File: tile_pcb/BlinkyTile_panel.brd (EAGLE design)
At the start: 220.1 x 170 mm, 210 parts

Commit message: Rev M panel from Sam
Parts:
- removed C1: .1uF, adafruit:C0603
- removed E$1, E$10, E$11, E$12, E$13, E$14, E$15, E$2, E$21, E$22, E$3, E$4, E$47, E$48, E$5, E$55, E$6, E$7, E$8, E$9: (no value), dodocohedreled:MOUSE_BITE_1
- removed E$16, E$17, E$19, E$20: (no value), dodocohedreled:MOUSE_BITE
- removed E$18: (no value), Sam-Lib:DUPONT-4P
- removed PROG, PROG1: (no value), solpad:SE14
- removed R1: 75, adafruit:R0603
- removed R2: 10k, adafruit:R0603
- removed U$2, U$3, U$4, U$5, U$6, U$91: D_EDGEMOD, dodocohedreled:D_EDGE_SLOT_MOD
- removed U$7: WS2822S_LED, blinkinlabs:WS2822S_LED
- added C4: .1uF, adafruit:C0603
- added E$100, E$101, E$102, E$103, E$104, E$105, E$106, E$107, E$108, E$109, E$110, E$111, E$112, E$113, E$114, E$115, E$116, E$117, E$118, E$119, E$120, E$121, E$122, E$123, E$124, E$125, E$126, E$127, E$128, E$129, E$130, E$131, E$132, E$133, E$134, E$135, E$136, E$137, E$138, E$139, E$140, E$141, E$142, E$143, E$144, E$145, E$146, E$147, E$148, E$149, E$150, E$151, E$152, E$153, E$154, E$155, E$156, E$157, E$158, E$159, E$160, E$161, E$162, E$163, E$164, E$165, E$166, E$167, E$168, E$169, E$170, E$171, E$172, E$173, E$174, E$175, E$176, E$177, E$178, E$179, E$180, E$181, E$182, E$183, E$184, E$185, E$186, E$187, E$188, E$189, E$190, E$191, E$192, E$193, E$199, E$200, E$202, E$203, E$81, E$82, E$83, E$84, E$85, E$86, E$87, E$88, E$89, E$90, E$91, E$92, E$93, E$94, E$95, E$96, E$97, E$98, E$99: (no value), dodocohedreled:MOUSE_BITE_1
- added E$201, E$204: (no value), dodocohedreled:4-PIN_DUPONT
- added E$205, E$206, E$207, E$208, E$209, E$210, E$211, E$212, E$213, E$214, E$215, E$216, E$217, E$218: (no value), dodocohedreled:BLINKYTILE
- added E$219: (no value), dodocohedreled:BLINKYTILELOGO
- added E$220, E$225: (no value), dodocohedreled:BLINKINLABSLOGO
- added E$221, E$222, E$223, E$224: (no value), SparkFun-Aesthetics:FIDUCIAL-1X2
- added PROG2, PROG3: (no value), solpad:SE14
- added R7: 75, adafruit:R0603
- added R8: 10k, adafruit:R0603
- added U$20, U$21, U$22, U$23, U$93, U$94: D_EDGEMOD, dodocohedreled:D_EDGE_SLOT_MOD
- added U$24: WS2822S_LED, blinkinlabs:WS2822S_LED
- E$76: device Sam-Lib:DUPONT-4P -> dodocohedreled:MOUSE_BITE_1
- E$77, E$78, E$79, E$80: device SparkFun-Aesthetics:FIDUCIAL-1X2 -> dodocohedreled:MOUSE_BITE_1
- moved E$67 207.0 mm to (105.3, 30.9), turned to 288 degrees
- moved E$80 202.4 mm to (78.3, 52.4), turned to 252 degrees
- moved E$70 188.5 mm to (81.0, 48.5), turned to 0 degrees
- moved E$73 184.2 mm to (81.0, 48.5), turned to 0 degrees
- moved U$44 182.5 mm to (-74.2, 66.8), turned to 252 degrees
- moved U$86 182.5 mm to (74.2, -66.8), turned to 72 degrees
- moved E$32 181.3 mm to (-105.3, 30.9), turned to 72 degrees
- moved E$72 174.3 mm to (105.3, 30.9), turned to 288 degrees
- moved E$78 164.8 mm to (39.0, 80.9), turned to 36 degrees
- moved U$46 160.0 mm to (-66.5, 43.0), turned to 324 degrees
- moved U$88 160.0 mm to (66.5, -43.0), turned to 144 degrees
- moved E$71 159.1 mm to (56.7, 30.9), turned to 72 degrees
- moved E$74 158.8 mm to (29.7, 52.4)
- moved U$43 156.7 mm to (-54.0, 81.5), turned to 180 degrees
- moved U$85 156.7 mm to (54.0, -81.5), turned to 0 degrees
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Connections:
- removed net 5V: R1.1, U$2.P$2, U$2.P$4, U$2.P$7, U$2.P$9, U$2.PWRVIA1, U$2.PWRVIA3, U$2.PWRVIA4, U$2.PWRVIA6, U$3.P$2, U$3.P$4, U$3.P$7, U$3.P$9, U$3.PWRVIA1, U$3.PWRVIA3, U$3.PWRVIA4, U$3.PWRVIA6, U$4.P$2, U$4.P$4, U$4.P$7, U$4.P$9, U$4.PWRVIA1, U$4.PWRVIA3, U$4.PWRVIA4, U$4.PWRVIA6, U$5.P$2, U$5.P$4, U$5.P$7, U$5.P$9, U$5.PWRVIA1, U$5.PWRVIA3, U$5.PWRVIA4, U$5.PWRVIA6, U$6.P$2, U$6.P$4, U$6.P$7, U$6.P$9, U$6.PWRVIA1, U$6.PWRVIA3, U$6.PWRVIA4, U$6.PWRVIA6, U$7.6
- removed net 5V1: R3.1, U$1.P$2, U$1.P$4, U$1.P$7, U$1.P$9, U$1.PWRVIA1, U$1.PWRVIA3, U$1.PWRVIA4, U$1.PWRVIA6, U$10.P$2, U$10.P$4, U$10.P$7, U$10.P$9, U$10.PWRVIA1, U$10.PWRVIA3, U$10.PWRVIA4, U$10.PWRVIA6, U$11.P$2, U$11.P$4, U$11.P$7, U$11.P$9, U$11.PWRVIA1, U$11.PWRVIA3, U$11.PWRVIA4, U$11.PWRVIA6, U$12.6, U$8.P$2, U$8.P$4, U$8.P$7, U$8.P$9, U$8.PWRVIA1, U$8.PWRVIA3, U$8.PWRVIA4, U$8.PWRVIA6, U$9.P$2, U$9.P$4, U$9.P$7, U$9.P$9, U$9.PWRVIA1, U$9.PWRVIA3, U$9.PWRVIA4, U$9.PWRVIA6
- removed net ADRI: U$7.2
- removed net DATA: R2.2, U$2.P$3, U$2.P$8, U$2.SIGVIA1, U$2.SIGVIA3, U$3.P$3, U$3.P$8, U$3.SIGVIA1, U$3.SIGVIA3, U$4.P$3, U$4.P$8, U$4.SIGVIA1, U$4.SIGVIA3, U$5.P$3, U$5.P$8, U$5.SIGVIA1, U$5.SIGVIA3, U$6.P$3, U$6.P$8, U$6.SIGVIA1, U$6.SIGVIA3
- removed net GND: C1.2, U$2.GNDVIA1, U$2.GNDVIA3, U$2.GNDVIA4, U$2.GNDVIA6, U$2.P$1, U$2.P$10, U$2.P$5, U$2.P$6, U$3.GNDVIA1, U$3.GNDVIA3, U$3.GNDVIA4, U$3.GNDVIA6, U$3.P$1, U$3.P$10, U$3.P$5, U$3.P$6, U$4.GNDVIA1, U$4.GNDVIA3, U$4.GNDVIA4, U$4.GNDVIA6, U$4.P$1, U$4.P$10, U$4.P$5, U$4.P$6, U$5.GNDVIA1, U$5.GNDVIA3, U$5.GNDVIA4, U$5.GNDVIA6, U$5.P$1, U$5.P$10, U$5.P$5, U$5.P$6, U$6.GNDVIA1, U$6.GNDVIA3, U$6.GNDVIA4, U$6.GNDVIA6, U$6.P$1, U$6.P$10, U$6.P$5, U$6.P$6, U$7.4
- removed net N$1: C1.1, R1.2, U$7.3
- removed net N$2: R2.1, U$7.1
- removed net S$1: E$18.P$2, U$91.P$3
- removed net S$10: E$18.P$3, PROG.MP
- removed net S$2: E$18.P$4, U$91.P$1, U$91.P$5
- removed net S$3: E$76.P$4, U$19.P$1, U$19.P$5
- removed net S$4: E$76.P$2, U$19.P$3
- removed net S$5: E$76.P$3, PROG1.MP
- removed net VCC: E$18.P$1, U$91.P$7, U$91.P$9
- removed net VCC1: E$76.P$1, U$19.P$7, U$19.P$9
- new net 5V15: R29.1, U$85.P$2, U$85.P$4, U$85.P$7, U$85.P$9, U$85.PWRVIA1, U$85.PWRVIA3, U$85.PWRVIA4, U$85.PWRVIA6, U$86.P$2, U$86.P$4, U$86.P$7, U$86.P$9, U$86.PWRVIA1, U$86.PWRVIA3, U$86.PWRVIA4, U$86.PWRVIA6, U$87.P$2, U$87.P$4, U$87.P$7, U$87.P$9, U$87.PWRVIA1, U$87.PWRVIA3, U$87.PWRVIA4, U$87.PWRVIA6, U$88.P$2, U$88.P$4, U$88.P$7, U$88.P$9, U$88.PWRVIA1, U$88.PWRVIA3, U$88.PWRVIA4, U$88.PWRVIA6, U$89.P$2, U$89.P$4, U$89.P$7, U$89.P$9, U$89.PWRVIA1, U$89.PWRVIA3, U$89.PWRVIA4, U$89.PWRVIA6, U$90.6
- new net 5V3: R5.1, U$13.P$2, U$13.P$4, U$13.P$7, U$13.P$9, U$13.PWRVIA1, U$13.PWRVIA3, U$13.PWRVIA4, U$13.PWRVIA6, U$14.P$2, U$14.P$4, U$14.P$7, U$14.P$9, U$14.PWRVIA1, U$14.PWRVIA3, U$14.PWRVIA4, U$14.PWRVIA6, U$15.P$2, U$15.P$4, U$15.P$7, U$15.P$9, U$15.PWRVIA1, U$15.PWRVIA3, U$15.PWRVIA4, U$15.PWRVIA6, U$16.P$2, U$16.P$4, U$16.P$7, U$16.P$9, U$16.PWRVIA1, U$16.PWRVIA3, U$16.PWRVIA4, U$16.PWRVIA6, U$17.P$2, U$17.P$4, U$17.P$7, U$17.P$9, U$17.PWRVIA1, U$17.PWRVIA3, U$17.PWRVIA4, U$17.PWRVIA6, U$18.6
- new net ADRI3: U$24.2
- new net DATA3: R8.2, U$19.P$3, U$19.P$8, U$19.SIGVIA1, U$19.SIGVIA3, U$20.P$3, U$20.P$8, U$20.SIGVIA1, U$20.SIGVIA3, U$21.P$3, U$21.P$8, U$21.SIGVIA1, U$21.SIGVIA3, U$22.P$3, U$22.P$8, U$22.SIGVIA1, U$22.SIGVIA3, U$23.P$3, U$23.P$8, U$23.SIGVIA1, U$23.SIGVIA3
- new net GND3: C4.2, U$19.GNDVIA1, U$19.GNDVIA3, U$19.GNDVIA4, U$19.GNDVIA6, U$19.P$1, U$19.P$10, U$19.P$5, U$19.P$6, U$20.GNDVIA1, U$20.GNDVIA3, U$20.GNDVIA4, U$20.GNDVIA6, U$20.P$1, U$20.P$10, U$20.P$5, U$20.P$6, U$21.GNDVIA1, U$21.GNDVIA3, U$21.GNDVIA4, U$21.GNDVIA6, U$21.P$1, U$21.P$10, U$21.P$5, U$21.P$6, U$22.GNDVIA1, U$22.GNDVIA3, U$22.GNDVIA4, U$22.GNDVIA6, U$22.P$1, U$22.P$10, U$22.P$5, U$22.P$6, U$23.GNDVIA1, U$23.GNDVIA3, U$23.GNDVIA4, U$23.GNDVIA6, U$23.P$1, U$23.P$10, U$23.P$5, U$23.P$6, U$24.4
- new net N$11: C4.1, R7.2, U$24.3
- new net N$12: R8.1, U$24.1
- new net S$11: E$204.P$2, U$94.P$3
- new net S$12: E$204.P$3, PROG3.MP
- new net S$6: E$201.P$4, U$93.P$1, U$93.P$5
- new net S$7: E$201.P$2, U$93.P$3
- new net S$8: E$201.P$3, PROG2.MP
- new net S$9: E$204.P$4, U$94.P$1, U$94.P$5
- new net VCC2: E$201.P$1, U$93.P$7, U$93.P$9
- new net VCC3: E$204.P$1, U$94.P$7, U$94.P$9
- net 5V10: now also R19.1, U$55.P$2, U$55.P$4, U$55.P$7, U$55.P$9, U$55.PWRVIA1, U$55.PWRVIA3, U$55.PWRVIA4, U$55.PWRVIA6, U$56.P$2, U$56.P$4, U$56.P$7, U$56.P$9, U$56.PWRVIA1, U$56.PWRVIA3, U$56.PWRVIA4, U$56.PWRVIA6, U$57.P$2, U$57.P$4, U$57.P$7, U$57.P$9, U$57.PWRVIA1, U$57.PWRVIA3, U$57.PWRVIA4, U$57.PWRVIA6, U$58.P$2, U$58.P$4, U$58.P$7, U$58.P$9, U$58.PWRVIA1, U$58.PWRVIA3, U$58.PWRVIA4, U$58.PWRVIA6, U$59.P$2, U$59.P$4, U$59.P$7, U$59.P$9, U$59.PWRVIA1, U$59.PWRVIA3, U$59.PWRVIA4, U$59.PWRVIA6, U$60.6; no longer R21.1, U$61.P$2, U$61.P$4, U$61.P$7, U$61.P$9, U$61.PWRVIA1, U$61.PWRVIA3, U$61.PWRVIA4, U$61.PWRVIA6, U$62.P$2, U$62.P$4, U$62.P$7, U$62.P$9, U$62.PWRVIA1, U$62.PWRVIA3, U$62.PWRVIA4, U$62.PWRVIA6, U$63.P$2, U$63.P$4, U$63.P$7, U$63.P$9, U$63.PWRVIA1, U$63.PWRVIA3, U$63.PWRVIA4, U$63.PWRVIA6, U$64.P$2, U$64.P$4, U$64.P$7, U$64.P$9, U$64.PWRVIA1, U$64.PWRVIA3, U$64.PWRVIA4, U$64.PWRVIA6, U$65.P$2, U$65.P$4, U$65.P$7, U$65.P$9, U$65.PWRVIA1, U$65.PWRVIA3, U$65.PWRVIA4, U$65.PWRVIA6, U$66.6
- net 5V11: now also R21.1, U$61.P$2, U$61.P$4, U$61.P$7, U$61.P$9, U$61.PWRVIA1, U$61.PWRVIA3, U$61.PWRVIA4, U$61.PWRVIA6, U$62.P$2, U$62.P$4, U$62.P$7, U$62.P$9, U$62.PWRVIA1, U$62.PWRVIA3, U$62.PWRVIA4, U$62.PWRVIA6, U$63.P$2, U$63.P$4, U$63.P$7, U$63.P$9, U$63.PWRVIA1, U$63.PWRVIA3, U$63.PWRVIA4, U$63.PWRVIA6, U$64.P$2, U$64.P$4, U$64.P$7, U$64.P$9, U$64.PWRVIA1, U$64.PWRVIA3, U$64.PWRVIA4, U$64.PWRVIA6, U$65.P$2, U$65.P$4, U$65.P$7, U$65.P$9, U$65.PWRVIA1, U$65.PWRVIA3, U$65.PWRVIA4, U$65.PWRVIA6, U$66.6; no longer R23.1, U$67.P$2, U$67.P$4, U$67.P$7, U$67.P$9, U$67.PWRVIA1, U$67.PWRVIA3, U$67.PWRVIA4, U$67.PWRVIA6, U$68.P$2, U$68.P$4, U$68.P$7, U$68.P$9, U$68.PWRVIA1, U$68.PWRVIA3, U$68.PWRVIA4, U$68.PWRVIA6, U$69.P$2, U$69.P$4, U$69.P$7, U$69.P$9, U$69.PWRVIA1, U$69.PWRVIA3, U$69.PWRVIA4, U$69.PWRVIA6, U$70.P$2, U$70.P$4, U$70.P$7, U$70.P$9, U$70.PWRVIA1, U$70.PWRVIA3, U$70.PWRVIA4, U$70.PWRVIA6, U$71.P$2, U$71.P$4, U$71.P$7, U$71.P$9, U$71.PWRVIA1, U$71.PWRVIA3, U$71.PWRVIA4, U$71.PWRVIA6, U$72.6
- net 5V12: now also R23.1, U$67.P$2, U$67.P$4, U$67.P$7, U$67.P$9, U$67.PWRVIA1, U$67.PWRVIA3, U$67.PWRVIA4, U$67.PWRVIA6, U$68.P$2, U$68.P$4, U$68.P$7, U$68.P$9, U$68.PWRVIA1, U$68.PWRVIA3, U$68.PWRVIA4, U$68.PWRVIA6, U$69.P$2, U$69.P$4, U$69.P$7, U$69.P$9, U$69.PWRVIA1, U$69.PWRVIA3, U$69.PWRVIA4, U$69.PWRVIA6, U$70.P$2, U$70.P$4, U$70.P$7, U$70.P$9, U$70.PWRVIA1, U$70.PWRVIA3, U$70.PWRVIA4, U$70.PWRVIA6, U$71.P$2, U$71.P$4, U$71.P$7, U$71.P$9, U$71.PWRVIA1, U$71.PWRVIA3, U$71.PWRVIA4, U$71.PWRVIA6, U$72.6; no longer R25.1, U$73.P$2, U$73.P$4, U$73.P$7, U$73.P$9, U$73.PWRVIA1, U$73.PWRVIA3, U$73.PWRVIA4, U$73.PWRVIA6, U$74.P$2, U$74.P$4, U$74.P$7, U$74.P$9, U$74.PWRVIA1, U$74.PWRVIA3, U$74.PWRVIA4, U$74.PWRVIA6, U$75.P$2, U$75.P$4, U$75.P$7, U$75.P$9, U$75.PWRVIA1, U$75.PWRVIA3, U$75.PWRVIA4, U$75.PWRVIA6, U$76.P$2, U$76.P$4, U$76.P$7, U$76.P$9, U$76.PWRVIA1, U$76.PWRVIA3, U$76.PWRVIA4, U$76.PWRVIA6, U$77.P$2, U$77.P$4, U$77.P$7, U$77.P$9, U$77.PWRVIA1, U$77.PWRVIA3, U$77.PWRVIA4, U$77.PWRVIA6, U$78.6
- net 5V13: now also R25.1, U$73.P$2, U$73.P$4, U$73.P$7, U$73.P$9, U$73.PWRVIA1, U$73.PWRVIA3, U$73.PWRVIA4, U$73.PWRVIA6, U$74.P$2, U$74.P$4, U$74.P$7, U$74.P$9, U$74.PWRVIA1, U$74.PWRVIA3, U$74.PWRVIA4, U$74.PWRVIA6, U$75.P$2, U$75.P$4, U$75.P$7, U$75.P$9, U$75.PWRVIA1, U$75.PWRVIA3, U$75.PWRVIA4, U$75.PWRVIA6, U$76.P$2, U$76.P$4, U$76.P$7, U$76.P$9, U$76.PWRVIA1, U$76.PWRVIA3, U$76.PWRVIA4, U$76.PWRVIA6, U$77.P$2, U$77.P$4, U$77.P$7, U$77.P$9, U$77.PWRVIA1, U$77.PWRVIA3, U$77.PWRVIA4, U$77.PWRVIA6, U$78.6; no longer R27.1, U$79.P$2, U$79.P$4, U$79.P$7, U$79.P$9, U$79.PWRVIA1, U$79.PWRVIA3, U$79.PWRVIA4, U$79.PWRVIA6, U$80.P$2, U$80.P$4, U$80.P$7, U$80.P$9, U$80.PWRVIA1, U$80.PWRVIA3, U$80.PWRVIA4, U$80.PWRVIA6, U$81.P$2, U$81.P$4, U$81.P$7, U$81.P$9, U$81.PWRVIA1, U$81.PWRVIA3, U$81.PWRVIA4, U$81.PWRVIA6, U$82.P$2, U$82.P$4, U$82.P$7, U$82.P$9, U$82.PWRVIA1, U$82.PWRVIA3, U$82.PWRVIA4, U$82.PWRVIA6, U$83.P$2, U$83.P$4, U$83.P$7, U$83.P$9, U$83.PWRVIA1, U$83.PWRVIA3, U$83.PWRVIA4, U$83.PWRVIA6, U$84.6
- net 5V14: now also R27.1, U$79.P$2, U$79.P$4, U$79.P$7, U$79.P$9, U$79.PWRVIA1, U$79.PWRVIA3, U$79.PWRVIA4, U$79.PWRVIA6, U$80.P$2, U$80.P$4, U$80.P$7, U$80.P$9, U$80.PWRVIA1, U$80.PWRVIA3, U$80.PWRVIA4, U$80.PWRVIA6, U$81.P$2, U$81.P$4, U$81.P$7, U$81.P$9, U$81.PWRVIA1, U$81.PWRVIA3, U$81.PWRVIA4, U$81.PWRVIA6, U$82.P$2, U$82.P$4, U$82.P$7, U$82.P$9, U$82.PWRVIA1, U$82.PWRVIA3, U$82.PWRVIA4, U$82.PWRVIA6, U$83.P$2, U$83.P$4, U$83.P$7, U$83.P$9, U$83.PWRVIA1, U$83.PWRVIA3, U$83.PWRVIA4, U$83.PWRVIA6, U$84.6; no longer R29.1, U$85.P$2, U$85.P$4, U$85.P$7, U$85.P$9, U$85.PWRVIA1, U$85.PWRVIA3, U$85.PWRVIA4, U$85.PWRVIA6, U$86.P$2, U$86.P$4, U$86.P$7, U$86.P$9, U$86.PWRVIA1, U$86.PWRVIA3, U$86.PWRVIA4, U$86.PWRVIA6, U$87.P$2, U$87.P$4, U$87.P$7, U$87.P$9, U$87.PWRVIA1, U$87.PWRVIA3, U$87.PWRVIA4, U$87.PWRVIA6, U$88.P$2, U$88.P$4, U$88.P$7, U$88.P$9, U$88.PWRVIA1, U$88.PWRVIA3, U$88.PWRVIA4, U$88.PWRVIA6, U$89.P$2, U$89.P$4, U$89.P$7, U$89.P$9, U$89.PWRVIA1, U$89.PWRVIA3, U$89.PWRVIA4, U$89.PWRVIA6, U$90.6
- net 5V2: now also R3.1, U$1.P$2, U$1.P$4, U$1.P$7, U$1.P$9, U$1.PWRVIA1, U$1.PWRVIA3, U$1.PWRVIA4, U$1.PWRVIA6, U$10.P$2, U$10.P$4, U$10.P$7, U$10.P$9, U$10.PWRVIA1, U$10.PWRVIA3, U$10.PWRVIA4, U$10.PWRVIA6, U$11.P$2, U$11.P$4, U$11.P$7, U$11.P$9, U$11.PWRVIA1, U$11.PWRVIA3, U$11.PWRVIA4, U$11.PWRVIA6, U$12.6, U$8.P$2, U$8.P$4, U$8.P$7, U$8.P$9, U$8.PWRVIA1, U$8.PWRVIA3, U$8.PWRVIA4, U$8.PWRVIA6, U$9.P$2, U$9.P$4, U$9.P$7, U$9.P$9, U$9.PWRVIA1, U$9.PWRVIA3, U$9.PWRVIA4, U$9.PWRVIA6; no longer R5.1, U$13.P$2, U$13.P$4, U$13.P$7, U$13.P$9, U$13.PWRVIA1, U$13.PWRVIA3, U$13.PWRVIA4, U$13.PWRVIA6, U$14.P$2, U$14.P$4, U$14.P$7, U$14.P$9, U$14.PWRVIA1, U$14.PWRVIA3, U$14.PWRVIA4, U$14.PWRVIA6, U$15.P$2, U$15.P$4, U$15.P$7, U$15.P$9, U$15.PWRVIA1, U$15.PWRVIA3, U$15.PWRVIA4, U$15.PWRVIA6, U$16.P$2, U$16.P$4, U$16.P$7, U$16.P$9, U$16.PWRVIA1, U$16.PWRVIA3, U$16.PWRVIA4, U$16.PWRVIA6, U$17.P$2, U$17.P$4, U$17.P$7, U$17.P$9, U$17.PWRVIA1, U$17.PWRVIA3, U$17.PWRVIA4, U$17.PWRVIA6, U$18.6
- net 5V4: now also R7.1, U$19.P$2, U$19.P$4, U$19.P$7, U$19.P$9, U$19.PWRVIA1, U$19.PWRVIA3, U$19.PWRVIA4, U$19.PWRVIA6, U$20.P$2, U$20.P$4, U$20.P$7, U$20.P$9, U$20.PWRVIA1, U$20.PWRVIA3, U$20.PWRVIA4, U$20.PWRVIA6, U$21.P$2, U$21.P$4, U$21.P$7, U$21.P$9, U$21.PWRVIA1, U$21.PWRVIA3, U$21.PWRVIA4, U$21.PWRVIA6, U$22.P$2, U$22.P$4, U$22.P$7, U$22.P$9, U$22.PWRVIA1, U$22.PWRVIA3, U$22.PWRVIA4, U$22.PWRVIA6, U$23.P$2, U$23.P$4, U$23.P$7, U$23.P$9, U$23.PWRVIA1, U$23.PWRVIA3, U$23.PWRVIA4, U$23.PWRVIA6, U$24.6; no longer R9.1, U$25.P$2, U$25.P$4, U$25.P$7, U$25.P$9, U$25.PWRVIA1, U$25.PWRVIA3, U$25.PWRVIA4, U$25.PWRVIA6, U$26.P$2, U$26.P$4, U$26.P$7, U$26.P$9, U$26.PWRVIA1, U$26.PWRVIA3, U$26.PWRVIA4, U$26.PWRVIA6, U$27.P$2, U$27.P$4, U$27.P$7, U$27.P$9, U$27.PWRVIA1, U$27.PWRVIA3, U$27.PWRVIA4, U$27.PWRVIA6, U$28.P$2, U$28.P$4, U$28.P$7, U$28.P$9, U$28.PWRVIA1, U$28.PWRVIA3, U$28.PWRVIA4, U$28.PWRVIA6, U$29.P$2, U$29.P$4, U$29.P$7, U$29.P$9, U$29.PWRVIA1, U$29.PWRVIA3, U$29.PWRVIA4, U$29.PWRVIA6, U$30.6
- net 5V5: now also R9.1, U$25.P$2, U$25.P$4, U$25.P$7, U$25.P$9, U$25.PWRVIA1, U$25.PWRVIA3, U$25.PWRVIA4, U$25.PWRVIA6, U$26.P$2, U$26.P$4, U$26.P$7, U$26.P$9, U$26.PWRVIA1, U$26.PWRVIA3, U$26.PWRVIA4, U$26.PWRVIA6, U$27.P$2, U$27.P$4, U$27.P$7, U$27.P$9, U$27.PWRVIA1, U$27.PWRVIA3, U$27.PWRVIA4, U$27.PWRVIA6, U$28.P$2, U$28.P$4, U$28.P$7, U$28.P$9, U$28.PWRVIA1, U$28.PWRVIA3, U$28.PWRVIA4, U$28.PWRVIA6, U$29.P$2, U$29.P$4, U$29.P$7, U$29.P$9, U$29.PWRVIA1, U$29.PWRVIA3, U$29.PWRVIA4, U$29.PWRVIA6, U$30.6; no longer R11.1, U$31.P$2, U$31.P$4, U$31.P$7, U$31.P$9, U$31.PWRVIA1, U$31.PWRVIA3, U$31.PWRVIA4, U$31.PWRVIA6, U$32.P$2, U$32.P$4, U$32.P$7, U$32.P$9, U$32.PWRVIA1, U$32.PWRVIA3, U$32.PWRVIA4, U$32.PWRVIA6, U$33.P$2, U$33.P$4, U$33.P$7, U$33.P$9, U$33.PWRVIA1, U$33.PWRVIA3, U$33.PWRVIA4, U$33.PWRVIA6, U$34.P$2, U$34.P$4, U$34.P$7, U$34.P$9, U$34.PWRVIA1, U$34.PWRVIA3, U$34.PWRVIA4, U$34.PWRVIA6, U$35.P$2, U$35.P$4, U$35.P$7, U$35.P$9, U$35.PWRVIA1, U$35.PWRVIA3, U$35.PWRVIA4, U$35.PWRVIA6, U$36.6
- net 5V6: now also R11.1, U$31.P$2, U$31.P$4, U$31.P$7, U$31.P$9, U$31.PWRVIA1, U$31.PWRVIA3, U$31.PWRVIA4, U$31.PWRVIA6, U$32.P$2, U$32.P$4, U$32.P$7, U$32.P$9, U$32.PWRVIA1, U$32.PWRVIA3, U$32.PWRVIA4, U$32.PWRVIA6, U$33.P$2, U$33.P$4, U$33.P$7, U$33.P$9, U$33.PWRVIA1, U$33.PWRVIA3, U$33.PWRVIA4, U$33.PWRVIA6, U$34.P$2, U$34.P$4, U$34.P$7, U$34.P$9, U$34.PWRVIA1, U$34.PWRVIA3, U$34.PWRVIA4, U$34.PWRVIA6, U$35.P$2, U$35.P$4, U$35.P$7, U$35.P$9, U$35.PWRVIA1, U$35.PWRVIA3, U$35.PWRVIA4, U$35.PWRVIA6, U$36.6; no longer R13.1, U$37.P$2, U$37.P$4, U$37.P$7, U$37.P$9, U$37.PWRVIA1, U$37.PWRVIA3, U$37.PWRVIA4, U$37.PWRVIA6, U$38.P$2, U$38.P$4, U$38.P$7, U$38.P$9, U$38.PWRVIA1, U$38.PWRVIA3, U$38.PWRVIA4, U$38.PWRVIA6, U$39.P$2, U$39.P$4, U$39.P$7, U$39.P$9, U$39.PWRVIA1, U$39.PWRVIA3, U$39.PWRVIA4, U$39.PWRVIA6, U$40.P$2, U$40.P$4, U$40.P$7, U$40.P$9, U$40.PWRVIA1, U$40.PWRVIA3, U$40.PWRVIA4, U$40.PWRVIA6, U$41.P$2, U$41.P$4, U$41.P$7, U$41.P$9, U$41.PWRVIA1, U$41.PWRVIA3, U$41.PWRVIA4, U$41.PWRVIA6, U$42.6
- net 5V7: now also R13.1, U$37.P$2, U$37.P$4, U$37.P$7, U$37.P$9, U$37.PWRVIA1, U$37.PWRVIA3, U$37.PWRVIA4, U$37.PWRVIA6, U$38.P$2, U$38.P$4, U$38.P$7, U$38.P$9, U$38.PWRVIA1, U$38.PWRVIA3, U$38.PWRVIA4, U$38.PWRVIA6, U$39.P$2, U$39.P$4, U$39.P$7, U$39.P$9, U$39.PWRVIA1, U$39.PWRVIA3, U$39.PWRVIA4, U$39.PWRVIA6, U$40.P$2, U$40.P$4, U$40.P$7, U$40.P$9, U$40.PWRVIA1, U$40.PWRVIA3, U$40.PWRVIA4, U$40.PWRVIA6, U$41.P$2, U$41.P$4, U$41.P$7, U$41.P$9, U$41.PWRVIA1, U$41.PWRVIA3, U$41.PWRVIA4, U$41.PWRVIA6, U$42.6; no longer R15.1, U$43.P$2, U$43.P$4, U$43.P$7, U$43.P$9, U$43.PWRVIA1, U$43.PWRVIA3, U$43.PWRVIA4, U$43.PWRVIA6, U$44.P$2, U$44.P$4, U$44.P$7, U$44.P$9, U$44.PWRVIA1, U$44.PWRVIA3, U$44.PWRVIA4, U$44.PWRVIA6, U$45.P$2, U$45.P$4, U$45.P$7, U$45.P$9, U$45.PWRVIA1, U$45.PWRVIA3, U$45.PWRVIA4, U$45.PWRVIA6, U$46.P$2, U$46.P$4, U$46.P$7, U$46.P$9, U$46.PWRVIA1, U$46.PWRVIA3, U$46.PWRVIA4, U$46.PWRVIA6, U$47.P$2, U$47.P$4, U$47.P$7, U$47.P$9, U$47.PWRVIA1, U$47.PWRVIA3, U$47.PWRVIA4, U$47.PWRVIA6, U$48.6
- net 5V8: now also R15.1, U$43.P$2, U$43.P$4, U$43.P$7, U$43.P$9, U$43.PWRVIA1, U$43.PWRVIA3, U$43.PWRVIA4, U$43.PWRVIA6, U$44.P$2, U$44.P$4, U$44.P$7, U$44.P$9, U$44.PWRVIA1, U$44.PWRVIA3, U$44.PWRVIA4, U$44.PWRVIA6, U$45.P$2, U$45.P$4, U$45.P$7, U$45.P$9, U$45.PWRVIA1, U$45.PWRVIA3, U$45.PWRVIA4, U$45.PWRVIA6, U$46.P$2, U$46.P$4, U$46.P$7, U$46.P$9, U$46.PWRVIA1, U$46.PWRVIA3, U$46.PWRVIA4, U$46.PWRVIA6, U$47.P$2, U$47.P$4, U$47.P$7, U$47.P$9, U$47.PWRVIA1, U$47.PWRVIA3, U$47.PWRVIA4, U$47.PWRVIA6, U$48.6; no longer R17.1, U$49.P$2, U$49.P$4, U$49.P$7, U$49.P$9, U$49.PWRVIA1, U$49.PWRVIA3, U$49.PWRVIA4, U$49.PWRVIA6, U$50.P$2, U$50.P$4, U$50.P$7, U$50.P$9, U$50.PWRVIA1, U$50.PWRVIA3, U$50.PWRVIA4, U$50.PWRVIA6, U$51.P$2, U$51.P$4, U$51.P$7, U$51.P$9, U$51.PWRVIA1, U$51.PWRVIA3, U$51.PWRVIA4, U$51.PWRVIA6, U$52.P$2, U$52.P$4, U$52.P$7, U$52.P$9, U$52.PWRVIA1, U$52.PWRVIA3, U$52.PWRVIA4, U$52.PWRVIA6, U$53.P$2, U$53.P$4, U$53.P$7, U$53.P$9, U$53.PWRVIA1, U$53.PWRVIA3, U$53.PWRVIA4, U$53.PWRVIA6, U$54.6
- net 5V9: now also R17.1, U$49.P$2, U$49.P$4, U$49.P$7, U$49.P$9, U$49.PWRVIA1, U$49.PWRVIA3, U$49.PWRVIA4, U$49.PWRVIA6, U$50.P$2, U$50.P$4, U$50.P$7, U$50.P$9, U$50.PWRVIA1, U$50.PWRVIA3, U$50.PWRVIA4, U$50.PWRVIA6, U$51.P$2, U$51.P$4, U$51.P$7, U$51.P$9, U$51.PWRVIA1, U$51.PWRVIA3, U$51.PWRVIA4, U$51.PWRVIA6, U$52.P$2, U$52.P$4, U$52.P$7, U$52.P$9, U$52.PWRVIA1, U$52.PWRVIA3, U$52.PWRVIA4, U$52.PWRVIA6, U$53.P$2, U$53.P$4, U$53.P$7, U$53.P$9, U$53.PWRVIA1, U$53.PWRVIA3, U$53.PWRVIA4, U$53.PWRVIA6, U$54.6; no longer R19.1, U$55.P$2, U$55.P$4, U$55.P$7, U$55.P$9, U$55.PWRVIA1, U$55.PWRVIA3, U$55.PWRVIA4, U$55.PWRVIA6, U$56.P$2, U$56.P$4, U$56.P$7, U$56.P$9, U$56.PWRVIA1, U$56.PWRVIA3, U$56.PWRVIA4, U$56.PWRVIA6, U$57.P$2, U$57.P$4, U$57.P$7, U$57.P$9, U$57.PWRVIA1, U$57.PWRVIA3, U$57.PWRVIA4, U$57.PWRVIA6, U$58.P$2, U$58.P$4, U$58.P$7, U$58.P$9, U$58.PWRVIA1, U$58.PWRVIA3, U$58.PWRVIA4, U$58.PWRVIA6, U$59.P$2, U$59.P$4, U$59.P$7, U$59.P$9, U$59.PWRVIA1, U$59.PWRVIA3, U$59.PWRVIA4, U$59.PWRVIA6, U$60.6
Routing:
- net GND3: track 0.00 -> 111.7 mm, vias 0 -> 19
- net GND: track 111.7 -> 0.00 mm, vias 19 -> 0
- net DATA: track 15.3 -> 0.00 mm
- net DATA3: track 0.00 -> 15.3 mm
- net S$10: track 14.5 -> 0.00 mm
- net S$5: track 14.5 -> 0.00 mm
- net S$8: track 0.00 -> 13.8 mm
- net S$12: track 0.00 -> 13.8 mm
- net ADRI3: track 0.00 -> 5.78 mm, vias 0 -> 1
- net ADRI: track 5.78 -> 0.00 mm, vias 1 -> 0
- net S$11: track 0.00 -> 4.88 mm
- net S$7: track 0.00 -> 4.88 mm
- net S$1: track 4.88 -> 0.00 mm
- net S$4: track 4.88 -> 0.00 mm
- net N$11: track 0.00 -> 3.70 mm
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- added copper zone on layer 16, net 5V15
- added copper zone on layer 16, net 5V3
- added copper zone on layer 1, net DATA3
- added copper zone on layer 1, net GND3
- added copper zone on layer 1, net N$10
- added copper zone on layer 1, net S$6
- added copper zone on layer 1, net S$9
- added copper zone on layer 16, net VCC2
- added copper zone on layer 16, net VCC3
- removed copper zone on layer 16, net 5V
- removed copper zone on layer 16, net 5V1
- removed copper zone on layer 1, net DATA
- removed copper zone on layer 1, net GND
- removed copper zone on layer 1, net N$4
- removed copper zone on layer 1, net S$2
- removed copper zone on layer 1, net S$3
- removed copper zone on layer 16, net VCC
- removed copper zone on layer 16, net VCC1
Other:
- board size 220.1 x 170 mm -> 230 x 175 mm
- board text added: "ADR"
- board text added: "SIG"
- board text removed: "-- by --"
- board text removed: "ADDR"
- board text removed: "ADDRESS"
- board text removed: "Blinkinlabs"
- board text removed: "Blinkinlabs.com"
- board text removed: "BlinkyTile"
- board text removed: "BlinkyTile by"
- board text removed: "Break here"
- board text removed: "Build Your Own Dynamic Light Sculptures"
- board text removed: "Designed by: Matt Mets, Ethan Hartman, Sam Choy, Honghong Lu"
- board text removed: "blinkytile.com"

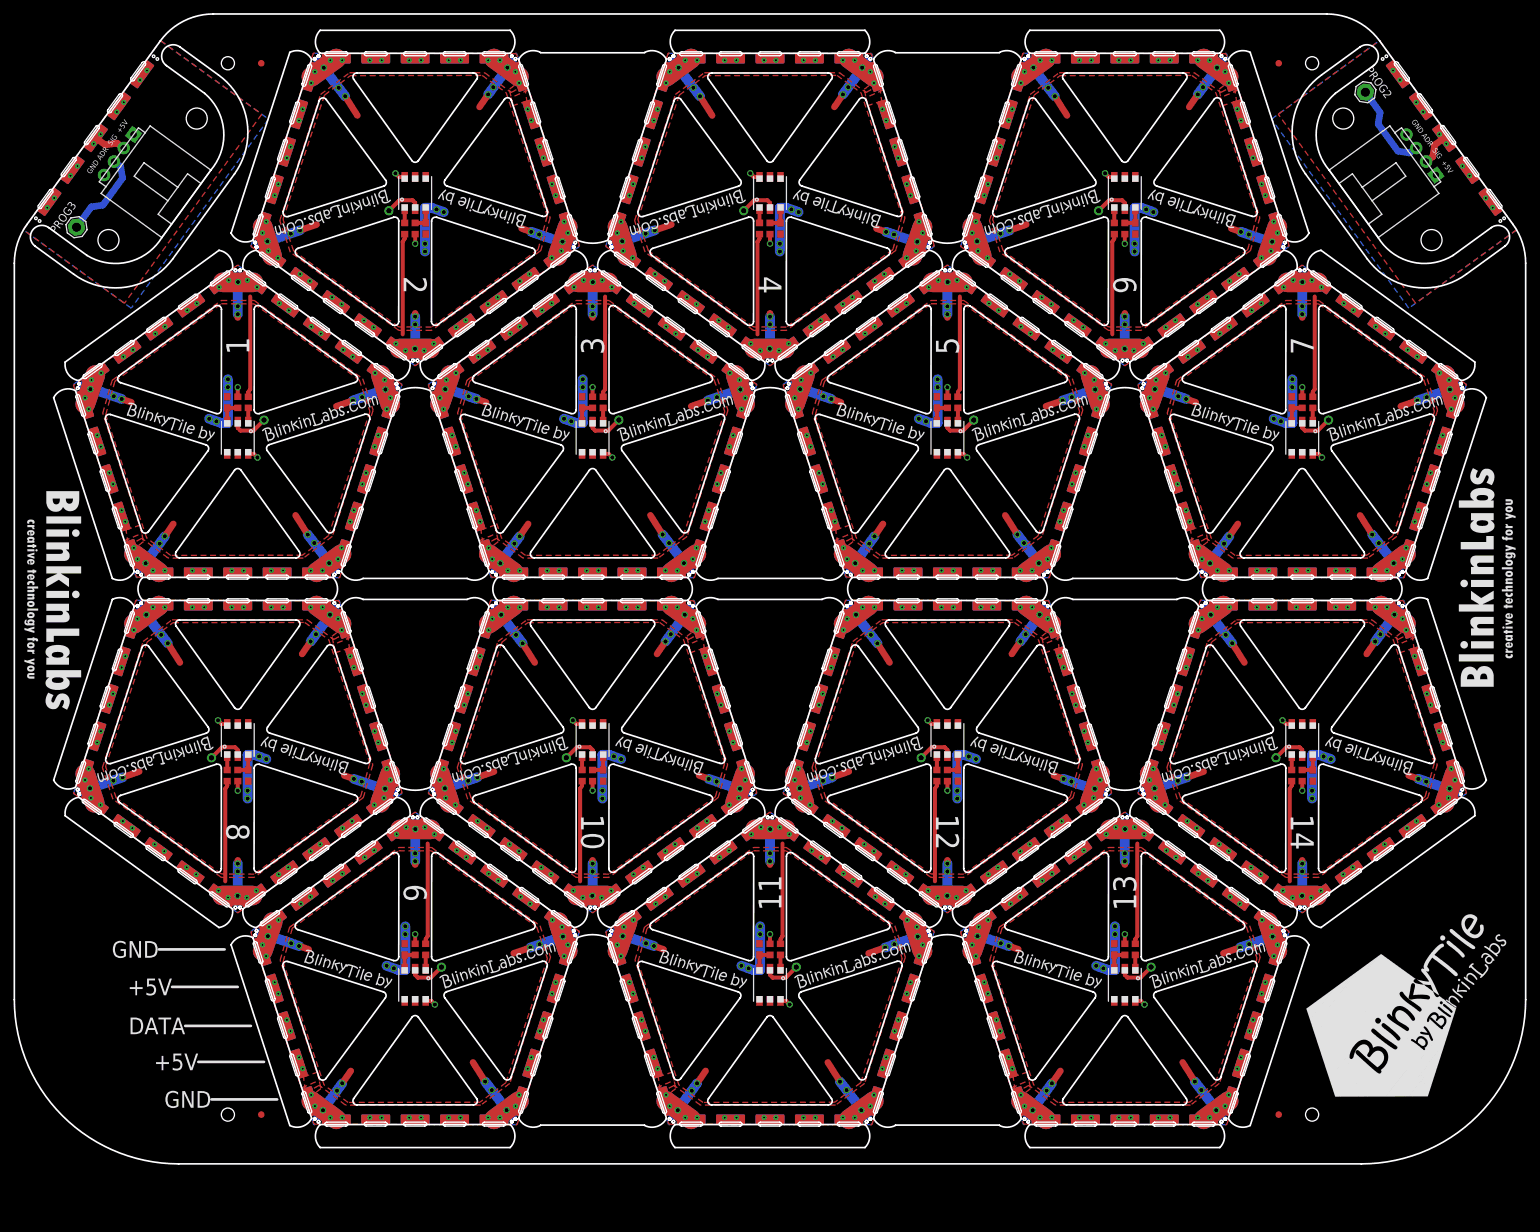
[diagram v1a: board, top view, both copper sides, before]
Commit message: New panel artwork
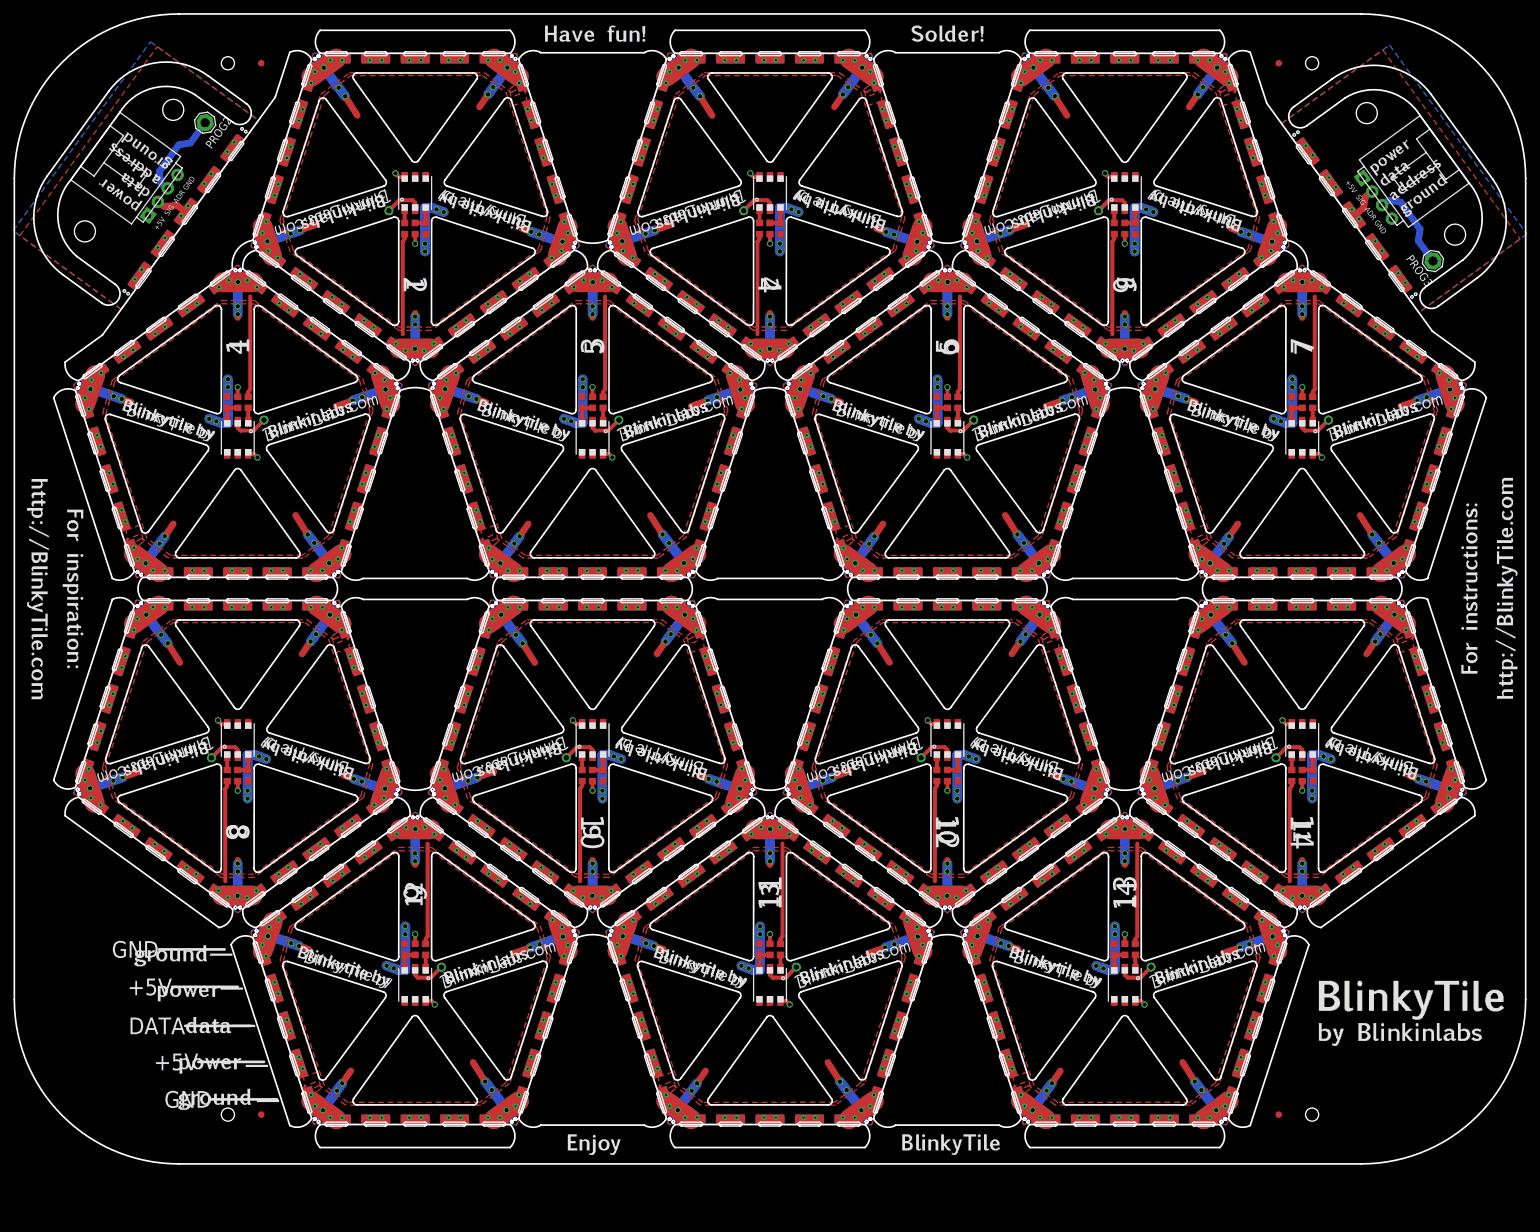
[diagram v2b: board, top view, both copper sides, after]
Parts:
- removed E$219: (no value), dodocohedreled:BLINKYTILELOGO
- removed E$220, E$225: (no value), dodocohedreled:BLINKINLABSLOGO
- moved E$203 209.7 mm to (98.0, 44.6), turned to 216 degrees
- moved E$199 209.7 mm to (-98.0, 45.1), turned to 144 degrees
- moved PROG3 206.5 mm to (100.9, 49.9), turned to 306 degrees
- moved U$94 191.9 mm to (88.3, 56.4), turned to 306 degrees
- moved U$93 191.9 mm to (-88.3, 56.9), turned to 54 degrees
- moved E$204 191.6 mm to (92.4, 59.4), turned to 306 degrees
- moved E$201 191.6 mm to (-92.4, 59.9), turned to 54 degrees
- moved PROG2 176.6 mm to (-86.0, 71.0), turned to 54 degrees
- moved E$202 174.0 mm to (80.1, 69.3), turned to 36 degrees
- moved E$200 173.9 mm to (-80.1, 69.8), turned to 324 degrees
- renumbered E$222 to E$1, E$223 to E$2
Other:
- outline, holes or cut-outs redrawn
